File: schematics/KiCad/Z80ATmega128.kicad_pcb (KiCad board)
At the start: 2 copper layers, 172.7 x 124.5 mm, 94 parts, among them J1 AVR-ISP-6, J2 Serial I/O, J2 Serial0, J3 Serial1, J4 DC 5V, J5 Z80[1..20], J6 DC 5V, J7 Z80[21..40], J8 Micro_SD_Card_Det_Hirose_DM3AT, SW1 POWER, SW2 RESET, U1 74HC125, U10 74HC32, U11 74HC74, U12 LP2950-3.3, U13 74HC132, U14 74HC4050, U2 74AC573, U3 74HCT574, U4 74HC04, U5 74HC125, U6 74HC244, U7 74HCT245, U8 74HC32, U9 74HC08, Y1 16MHz, Y2 8MHz

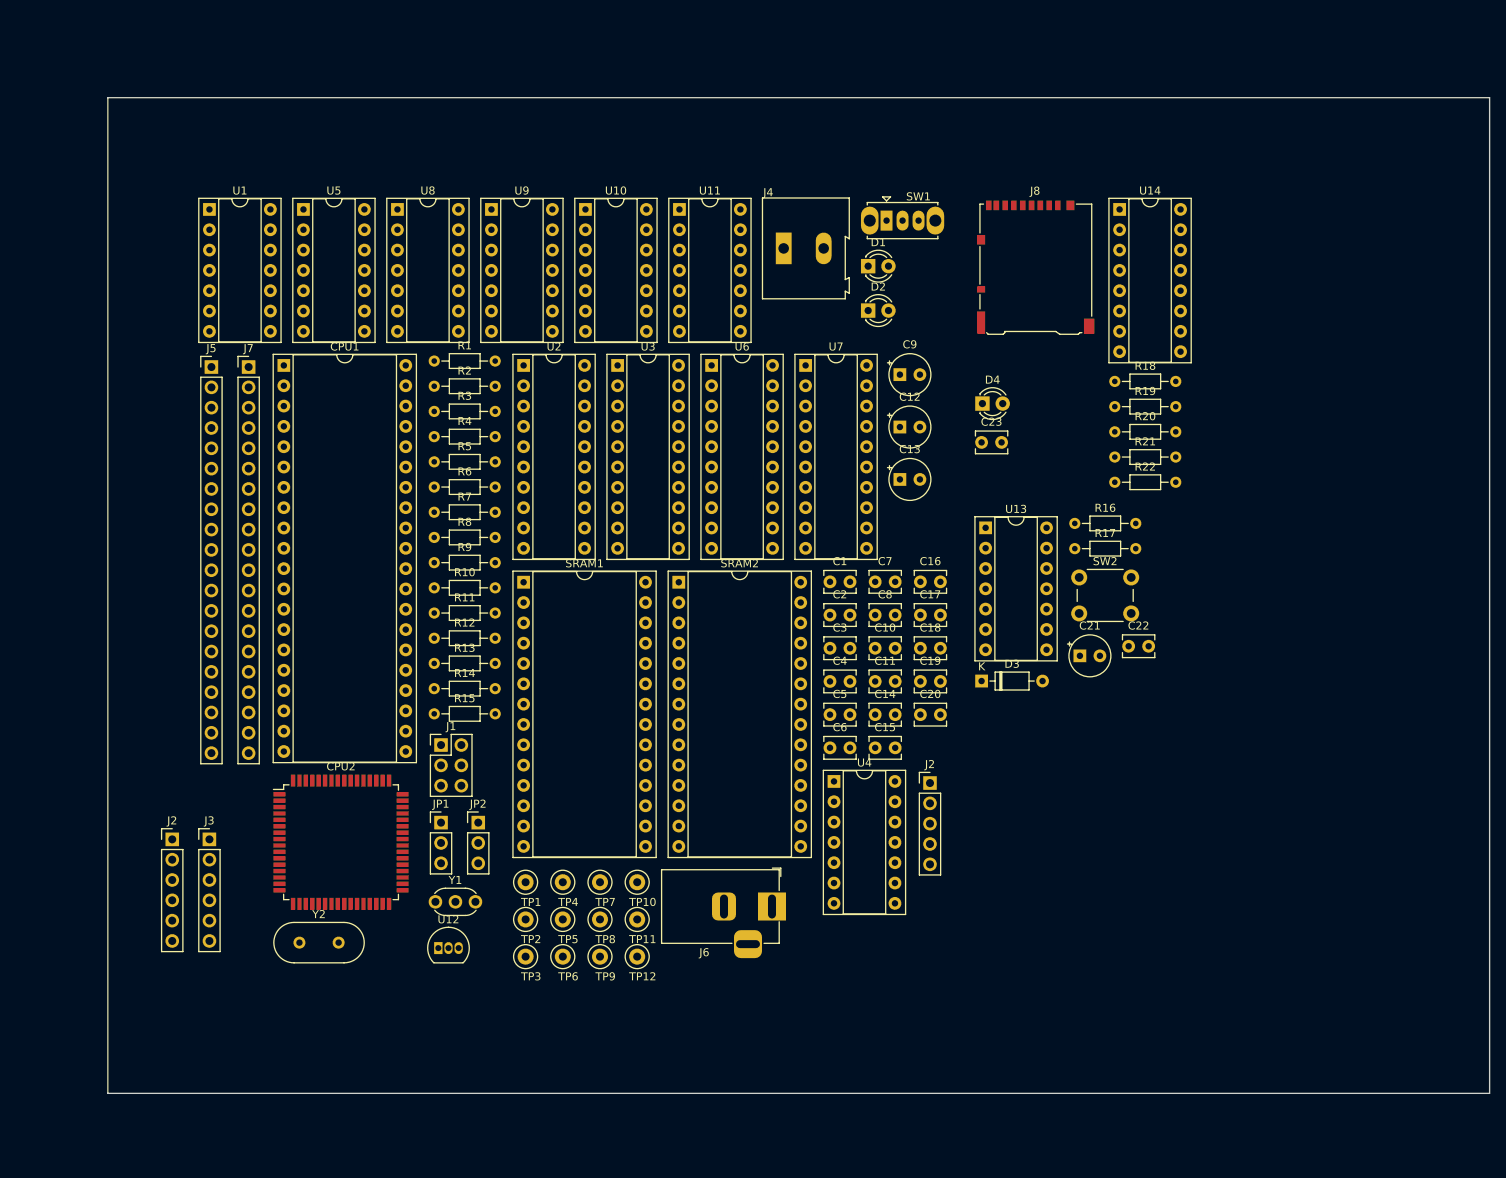
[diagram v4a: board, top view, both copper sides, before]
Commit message: Update Reset circuit and Serial interface
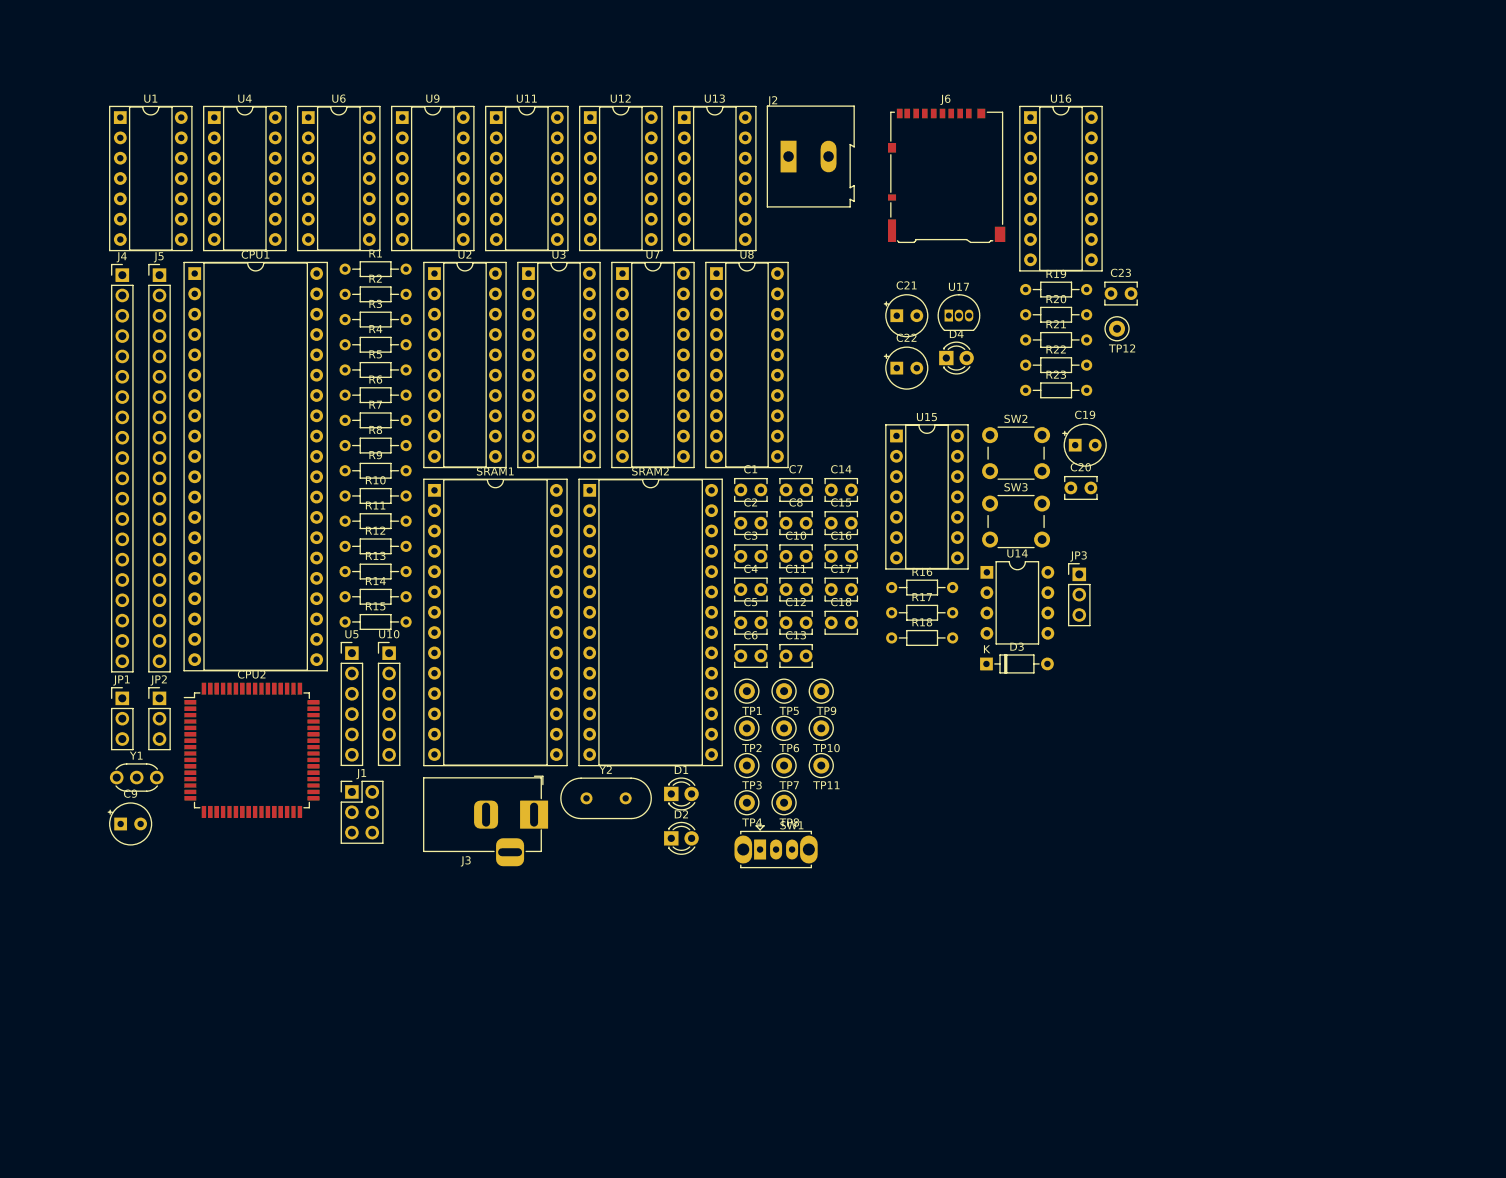
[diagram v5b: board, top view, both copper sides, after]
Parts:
- removed the J2 at (129.4, 111.1)
- removed the J2 at (34.7, 118.1)
- removed J7: Z80[21..40], Connector_PinHeader_2.54mm:PinHeader_1x20_P2.54mm_Vertical
- removed J8: Micro_SD_Card_Det_Hirose_DM3AT, Connector_Card:microSD_HC_Hirose_DM3AT-SF-PEJM5
- added J2: DC 5V, TerminalBlock:TerminalBlock_Altech_AK300-2_P5.00mm, F.Cu at (111.8, 32.8)
- added JP3: RESET SEL, Connector_PinHeader_2.54mm:PinHeader_1x03_P2.54mm_Vertical, F.Cu at (148.1, 85.0)
- added R23: 1K, Resistor_THT:R_Axial_DIN0204_L3.6mm_D1.6mm_P7.62mm_Horizontal, F.Cu at (141.4, 62.0)
- added SW3: RESET, Button_Switch_THT:SW_PUSH_6mm_H7.3mm, F.Cu at (136.9, 76.1)
- added U15: 74HC132, Package_DIP:DIP-14_W7.62mm_Socket, F.Cu at (125.2, 67.7)
- added U16: 74HC4050, Package_DIP:DIP-16_W7.62mm_Socket, F.Cu at (142.0, 27.9)
- added U17: LP2950-3.3, Package_TO_SOT_THT:TO-92_Inline, F.Cu at (131.8, 52.6)
- C12, C13: value 1u -> 0.1u; footprint Capacitor_THT:CP_Radial_Tantal_D5.0mm_P2.50mm -> Capacitor_THT:C_Disc_D3.8mm_W2.6mm_P2.50mm
- C19: value 0.1u -> 47u; footprint Capacitor_THT:C_Disc_D3.8mm_W2.6mm_P2.50mm -> Capacitor_THT:CP_Radial_Tantal_D5.0mm_P2.50mm
- C21: value 47u -> 1u
- C22: value 0.1u -> 1u; footprint Capacitor_THT:C_Disc_D3.8mm_W2.6mm_P2.50mm -> Capacitor_THT:CP_Radial_Tantal_D5.0mm_P2.50mm
- J3: value Serial1 -> DC 5V; footprint Connector_PinHeader_2.54mm:PinHeader_1x06_P2.54mm_Vertical -> Connector_BarrelJack:BarrelJack_Horizontal
- J4: value DC 5V -> Z80[1..20]; footprint TerminalBlock:TerminalBlock_Altech_AK300-2_P5.00mm -> Connector_PinHeader_2.54mm:PinHeader_1x20_P2.54mm_Vertical
- J5: value Z80[1..20] -> Z80[21..40]
- J6: value DC 5V -> Micro_SD_Card_Det_Hirose_DM3AT; footprint Connector_BarrelJack:BarrelJack_Horizontal -> Connector_Card:microSD_HC_Hirose_DM3AT-SF-PEJM5
- R17: value 100 -> 10K
- R18: value 10K -> 100
- R22: value 1K -> 10K
- TP8: value /INTRQ -> GND
- TP9: value GND -> /INTRQ
- U10: value 74HC32 -> AE-CH340E-TYPEC; footprint Package_DIP:DIP-14_W7.62mm_Socket -> Connector_PinHeader_2.54mm:PinHeader_1x06_P2.54mm_Vertical
- U11: value 74HC74 -> 74HC08
- U12: value LP2950-3.3 -> 74HC32; footprint Package_TO_SOT_THT:TO-92_Inline -> Package_DIP:DIP-14_W7.62mm_Socket
- U13: value 74HC132 -> 74HC74
- U14: value 74HC4050 -> DS1232; footprint Package_DIP:DIP-16_W7.62mm_Socket -> Package_DIP:DIP-8_W7.62mm
- U5: value 74HC125 -> AE-CH340E-TYPEC; footprint Package_DIP:DIP-14_W7.62mm_Socket -> Connector_PinHeader_2.54mm:PinHeader_1x06_P2.54mm_Vertical
- U6: value 74HC244 -> 74HC125; footprint Package_DIP:DIP-20_W7.62mm_Socket -> Package_DIP:DIP-14_W7.62mm_Socket
- U7: value 74HCT245 -> 74HC244
- U8: value 74HC32 -> 74HCT245; footprint Package_DIP:DIP-14_W7.62mm_Socket -> Package_DIP:DIP-20_W7.62mm_Socket
- U9: value 74HC08 -> 74HC32
- moved U4 113.5 mm to (40.0, 27.9)
- moved C9 112.4 mm to (28.3, 116.2)
- moved U12 105.5 mm to (87.0, 27.9)
- moved TP12 98.8 mm to (152.8, 54.3)
- moved J6 94.0 mm to (131.5, 35.1)
- moved J4 82.7 mm to (28.5, 47.6)
- moved SW1 80.2 mm to (108.2, 119.4)
- moved D1 70.4 mm to (97.1, 112.4)
- moved D2 70.4 mm to (97.1, 118.0)
- moved U13 63.6 mm to (98.7, 27.9)
- moved U10 60.7 mm to (61.8, 94.8)
- moved U6 59.2 mm to (51.7, 27.9)
- moved U5 55.8 mm to (57.2, 94.8)
- moved U14 48.3 mm to (136.6, 84.7)
- moved C21 48.3 mm to (125.3, 52.7)
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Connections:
- C13 pad 1: +3.3V -> VCC
- C19 pad 1: VCC -> Net-(D3-A)
- C21 pad 1: Net-(D3-A) -> VCC
- C22 pad 1: VCC -> +3.3V
- J3 pad 1: unconnected-(J3-Pin_1-Pad1) -> Net-(J3-In)
- J3 pad 2: RXD1 -> GND
- J3 pad 3: TXD1 -> (no net)
- J4 pad 1: GND -> A11
- J4 pad 2: Net-(J4-Pin_2) -> A12
- J5 pad 1: A11 -> A10
- J5 pad 10: DB6 -> A1
- J5 pad 11: VCC -> A0
- J5 pad 12: DB2 -> GND
- J5 pad 13: DB7 -> /RFSH
- J5 pad 14: DB0 -> /M1
- J5 pad 15: DB1 -> /Z80_RESET
- J5 pad 16: /XINT -> /BUSRQ
- J5 pad 17: /NMI -> /WAIT
- J5 pad 18: /HALT -> /BUSACK
- J5 pad 19: /MREQ -> /WR
- J5 pad 2: A12 -> A9
- J5 pad 20: /IORQ -> /RD
- J5 pad 3: A13 -> A8
- J5 pad 4: A14 -> A7
- J5 pad 5: A15 -> A6
- J5 pad 6: 4MHz -> A5
- J5 pad 7: DB4 -> A4
- J5 pad 8: DB3 -> A3
- J5 pad 9: DB5 -> A2
- J6 pad 1: Net-(J6-In) -> unconnected-(J6-DAT2-Pad1)
- J6 pad 2: GND -> Net-(D4-K)
- J6 pad 3: (no net) -> Net-(J6-CMD)
- JP2 pad 1: Net-(J6-In) -> Net-(J3-In)
- JP2 pad 2: VBUS -> Net-(#FLG01-pwr)
- JP2 pad 3: Net-(J4-Pin_2) -> Net-(J2-Pin_2)
- R16 pad 2: Net-(D3-A) -> Net-(JP3-B)
- R17 pad 1: Net-(R17-Pad1) -> VCC
- R18 pad 1: VCC -> Net-(R18-Pad1)
- R18 pad 2: SW -> Net-(D3-A)
- R19 pad 2: /SS -> SW
- R20 pad 1: MOSI -> VCC
- R20 pad 2: GND -> /SS
- R21 pad 1: SCK -> MOSI
- R22 pad 1: Net-(R22-Pad1) -> SCK
- R22 pad 2: Net-(D4-A) -> GND
- SW1 pad 2: VBUS -> Net-(#FLG01-pwr)
- SW2 pad 2: Net-(R17-Pad1) -> Net-(U14-/PBRST)
- TP3 pad 1: Net-(U7-CE) -> Net-(U8-CE)
- TP8 pad 1: /INTRQ -> GND
- TP9 pad 1: GND -> /INTRQ
- U10 pad 1: /WR -> unconnected-(U10-RTS-Pad1)
- U10 pad 2: /MREQ -> TXD1
- U10 pad 3: Net-(U1-Pad2) -> RXD1
- U10 pad 4: /MREQ -> Net-(#FLG01-pwr)
- U10 pad 5: /RD -> unconnected-(U10-CTS-Pad5)
- U10 pad 6: Net-(U1-Pad5) -> GND
- U11 pad 1: VCC -> /WAIT
- U11 pad 10: /CLRWAIT -> /INTRQ
- U11 pad 11: Net-(U11B-C) -> /Z80_RESET
- U11 pad 12: Net-(U11B-D) -> Net-(JP3-C)
- U11 pad 13: VCC -> /Reset//Z80_SWRST
- U11 pad 2: Net-(U11A-D) -> 4MHz
- U11 pad 3: Net-(U11A-C) -> Net-(U13B-C)
- U11 pad 4: VCC -> /IOWR
- U11 pad 5: 4MHz -> /MREQ
- U11 pad 6: Net-(U11A-D) -> Net-(U8-CE)
- U11 pad 8: Net-(U11B-~{Q}) -> Net-(U3-OE)
- U11 pad 9: /WAIT -> /IORD
- U12 pad 1: +3.3V -> /WR
- U12 pad 2: GND -> /MREQ
- U12 pad 3: VCC -> Net-(U1-Pad2)
- U13 pad 1: Net-(D3-A) -> VCC
- U13 pad 10: Net-(U13-Pad10) -> /CLRWAIT
- U13 pad 11: /Reset//AVR_RST -> Net-(U13B-C)
- U13 pad 12: Net-(U13-Pad12) -> Net-(U13B-D)
- U13 pad 13: Net-(U13-Pad12) -> VCC
- U13 pad 2: Net-(D3-A) -> Net-(U13A-D)
- U13 pad 3: Net-(U13-Pad3) -> Net-(U13A-C)
- U13 pad 4: Net-(U13-Pad3) -> VCC
- U13 pad 5: Net-(U13-Pad3) -> 4MHz
- U13 pad 6: Net-(U13-Pad10) -> Net-(U13A-D)
- U13 pad 8: Net-(U13-Pad12) -> Net-(U13B-~{Q})
- U13 pad 9: /Reset//ISP_RST -> /WAIT
- U14 pad 1: +3.3V -> Net-(U14-/PBRST)
- U14 pad 2: Net-(D4-K) -> GND
- U14 pad 3: /SS -> GND
- U14 pad 4: Net-(J8-CMD) -> GND
- U14 pad 5: MOSI -> unconnected-(U14-RST-Pad5)
- U14 pad 6: Net-(J8-CLK) -> Net-(JP3-B)
- U14 pad 7: SCK -> 4MHz
- U14 pad 8: GND -> VCC
- U4 pad 10: Net-(U11A-C) -> Net-(U13A-C)
- U5 pad 1: Net-(U4-Pad6) -> unconnected-(U5-RTS-Pad1)
- U5 pad 2: Net-(J2-Pin_2) -> Net-(U5-RXD)
- U5 pad 3: Net-(CPU2-PE0) -> Net-(U5-TXD)
- U5 pad 4: Net-(U4-Pad6) -> Net-(#FLG01-pwr)
- U5 pad 5: Net-(CPU2-PE1) -> unconnected-(U5-CTS-Pad5)
- U5 pad 6: Net-(J2-Pin_3) -> GND
- U6 pad 1: /BUSACK -> Net-(U4-Pad6)
- U6 pad 10: GND -> /BUSACK
- U6 pad 11: Net-(CPU2-PC7) -> Net-(SRAM1-~{OE})
- U6 pad 12: A11 -> /RD
- U6 pad 13: Net-(CPU2-PC6) -> /BUSACK
- U6 pad 14: A10 -> VCC
- U6 pad 2: Net-(CPU2-PC0) -> Net-(U5-TXD)
- U6 pad 3: A12 -> Net-(CPU2-PE0)
- U6 pad 4: Net-(CPU2-PC1) -> Net-(U4-Pad6)
- U6 pad 5: A13 -> Net-(CPU2-PE1)
- U6 pad 6: Net-(CPU2-PC2) -> Net-(U5-RXD)
- U6 pad 7: A14 -> GND
- U6 pad 8: Net-(CPU2-PC3) -> Net-(SRAM1-~{WE})
- U6 pad 9: A15 -> /WR
- U7 pad 1: /WR -> /BUSACK
- U7 pad 11: DB7 -> Net-(CPU2-PC7)
- U7 pad 12: DB6 -> A11
- U7 pad 13: DB5 -> Net-(CPU2-PC6)
- U7 pad 14: DB4 -> A10
- U7 pad 15: DB3 -> Net-(CPU2-PC5)
- U7 pad 16: DB2 -> A9
- U7 pad 17: DB1 -> Net-(CPU2-PC4)
- U7 pad 18: DB0 -> A8
- U7 pad 19: Net-(U7-CE) -> /BUSACK
- U7 pad 2: D0 -> Net-(CPU2-PC0)
- U7 pad 3: D1 -> A12
- U7 pad 4: D2 -> Net-(CPU2-PC1)
- U7 pad 5: D3 -> A13
- U7 pad 6: D4 -> Net-(CPU2-PC2)
- U7 pad 7: D5 -> A14
- U7 pad 8: D6 -> Net-(CPU2-PC3)
- U7 pad 9: D7 -> A15
- U8 pad 1: A7 -> /WR
- U8 pad 10: Net-(U11B-~{Q}) -> GND
- U8 pad 11: unconnected-(U8-Pad11) -> DB7
- U8 pad 12: GND -> DB6
- U8 pad 13: GND -> DB5
- U8 pad 14: VCC -> DB4
- U8 pad 2: /IORQ -> D0
- U8 pad 3: Net-(U10-Pad10) -> D1
- U8 pad 4: /M1 -> D2
- U8 pad 5: /IORQ -> D3
- U8 pad 6: /INTRQ -> D4
- U8 pad 7: GND -> D5
- U8 pad 8: Net-(U11B-D) -> D6
- U8 pad 9: /IORQ -> D7
- U9 pad 1: /WAIT -> A7
- U9 pad 10: /INTRQ -> Net-(U13B-~{Q})
- U9 pad 11: /Z80_RESET -> unconnected-(U9-Pad11)
- U9 pad 12: Net-(U13-Pad10) -> GND
- U9 pad 13: /Reset//Z80_SWRST -> GND
- U9 pad 2: 4MHz -> /IORQ
- U9 pad 3: Net-(U11B-C) -> Net-(U12-Pad10)
- U9 pad 4: /IOWR -> /M1
- U9 pad 5: /MREQ -> /IORQ
- U9 pad 6: Net-(U7-CE) -> /INTRQ
- U9 pad 8: Net-(U3-OE) -> Net-(U13B-D)
- U9 pad 9: /IORD -> /IORQ
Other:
- board outline removed
